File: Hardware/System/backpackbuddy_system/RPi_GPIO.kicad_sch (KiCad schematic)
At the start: 1 part, among them J6 RPi_GPIO

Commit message: pin matched everything
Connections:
- net 3v3: now reaches J6.1 (Pin_1)
- net 3v3: now also J6.17 (Pin_17)
- net GPIO15_RXD: now reaches J6.10 (Pin_10)
- net GPIO17: now reaches J6.11 (Pin_11)
- net GPIO18_PCM_CLK: now reaches J6.12 (Pin_12)
- net GPIO27: now reaches J6.13 (Pin_13)
- net GND: now reaches J6.14 (Pin_14)
- net GND: now also J6.20 (Pin_20), J6.25 (Pin_25), J6.30 (Pin_30), J6.34 (Pin_34), J6.39 (Pin_39), J6.6 (Pin_6), J6.9 (Pin_9)
- net GPIO22: now reaches J6.15 (Pin_15)
- net GPIO23: now reaches J6.16 (Pin_16)
- net GPIO24: now reaches J6.18 (Pin_18)
- net GPIO10_MOSI: now reaches J6.19 (Pin_19)
- net 5v: now reaches J6.2 (Pin_2)
- net 5v: now also J6.4 (Pin_4)
- net GPIO10_MISO: now reaches J6.21 (Pin_21)
- net GPIO25: now reaches J6.22 (Pin_22)
- net GPIO11_SCLK: now reaches J6.23 (Pin_23)
- net GPIO8_CE0: now reaches J6.24 (Pin_24)
- net GPIO7_CE1: now reaches J6.26 (Pin_26)
- net GPIO0_ID_SD: now reaches J6.27 (Pin_27)
- net GPIO1_ID_SE: now reaches J6.28 (Pin_28)
- net GPIO5: now reaches J6.29 (Pin_29)
- net GPIO6: now reaches J6.31 (Pin_31)
- net GPIO12_PWM0: now reaches J6.32 (Pin_32)
- net GPIO13_PWM1: now reaches J6.33 (Pin_33)
- net GPIO19_PCM_FS: now reaches J6.35 (Pin_35)
- net GPIO16: now reaches J6.36 (Pin_36)
- net GPIO26: now reaches J6.37 (Pin_37)
- net GPIO20_PCM_DIN: now reaches J6.38 (Pin_38)
- net GPIO21_PCM_DOUT: now reaches J6.40 (Pin_40)
- net GPIO14_TXD: now reaches J6.8 (Pin_8)

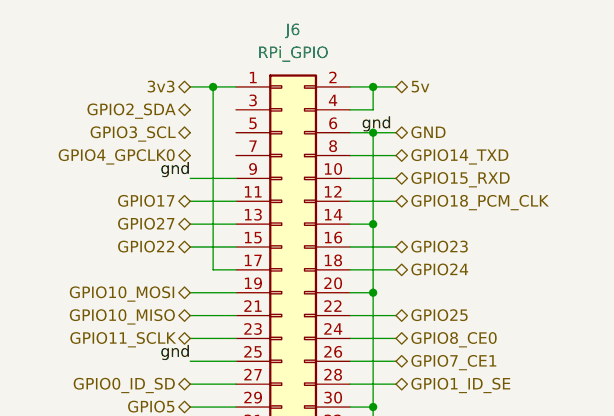
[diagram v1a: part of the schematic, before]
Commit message: pull down resistor to ESP reset
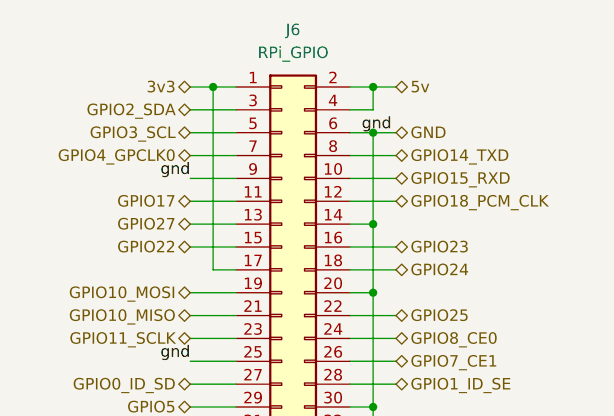
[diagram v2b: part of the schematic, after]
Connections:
- net GPIO2_SDA: now also J6.3 (Pin_3)
- net GPIO3_SCL: now also J6.5 (Pin_5)
- net GPIO4_GPCLK0: now also J6.7 (Pin_7)
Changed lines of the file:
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@@
+    (stroke (width 0) (type default) (color 0 0 0 0))
+  )
+  (wire (pts (xy 134.62 68.58) (xy 139.7 68.58))
     (stroke (width 0) (type default) (color 0 0 0 0))
   )
@@
     (stroke (width 0) (type default) (color 0 0 0 0))
   )
+  (wire (pts (xy 134.62 66.04) (xy 139.7 66.04))
+    (stroke (width 0) (type default) (color 0 0 0 0))
+  )
   (wire (pts (xy 152.4 63.5) (xy 154.94 63.5))
     (stroke (width 0) (type default) (color 0 0 0 0))
@@
     (stroke (width 0) (type default) (color 0 0 0 0))
   )
+  (wire (pts (xy 134.62 71.12) (xy 139.7 71.12))
+    (stroke (width 0) (type default) (color 0 0 0 0))
+  )

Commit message: decoupling caps
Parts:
- added C? (x4): 10uF, Capacitor_SMD:C_0805_2012Metric_Pad1.18x1.45mm_HandSolder, symbol Device:C
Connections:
- net GND: now also C?.2, C?.2, C?.2, C?.2
- new net +3V3: C?.1, C?.1
- new net +5V: C?.1, C?.1
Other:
- note added: "PI DECOUPLING CAPS"

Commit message: board outline redo
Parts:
- removed C?: 10uF, Capacitor_SMD:C_0805_2012Metric_Pad1.18x1.45mm_HandSolder, symbol Device:C
- gave numbers to parts that had none: 3
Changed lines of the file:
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@@
   (junction (at 154.94 86.36) (diameter 0) (color 0 0 0 0)
   )
-  (junction (at 187.96 40.64) (diameter 0) (color 0 0 0 0)
-  )
-  (junction (at 198.12 53.34) (diameter 0) (color 0 0 0 0)
-  )
   (wire (pts (xy 134.62 99.06) (xy 139.7 99.06))
     (stroke (width 0) (type default) (color 0 0 0 0))
@@
     (stroke (width 0) (type default) (color 0 0 0 0))
   )
-  (wire (pts (xy 198.12 50.8) (xy 198.12 53.34))
-    (stroke (width 0) (type default) (color 0 0 0 0))
-  )
-  (wire (pts (xy 187.96 39.37) (xy 187.96 40.64))
-    (stroke (width 0) (type default) (color 0 0 0 0))
-  )
   (wire (pts (xy 152.4 104.14) (xy 154.94 104.14))
     (stroke (width 0) (type default) (color 0 0 0 0))
@@
     (stroke (width 0) (type default) (color 0 0 0 0))
   )
-  (wire (pts (xy 187.96 40.64) (xy 187.96 43.18))
+  (wire (pts (xy 187.96 39.37) (xy 187.96 43.18))
     (stroke (width 0) (type default) (color 0 0 0 0))
   )
@@
     (stroke (width 0) (type default) (color 0 0 0 0))
   )
-  (wire (pts (xy 187.96 53.34) (xy 198.12 53.34))
-    (stroke (width 0) (type default) (color 0 0 0 0))
-  )
   (wire (pts (xy 152.4 91.44) (xy 157.48 91.44))
     (stroke (width 0) (type default) (color 0 0 0 0))
@@
     (stroke (width 0) (type default) (color 0 0 0 0))
   )
-  (wire (pts (xy 198.12 53.34) (xy 203.2 53.34))
+  (wire (pts (xy 187.96 53.34) (xy 203.2 53.34))
     (stroke (width 0) (type default) (color 0 0 0 0))
   )
@@
     (stroke (width 0) (type default) (color 0 0 0 0))
   )
-  (wire (pts (xy 198.12 40.64) (xy 187.96 40.64))
-    (stroke (width 0) (type default) (color 0 0 0 0))
-  )
   (wire (pts (xy 152.4 66.04) (xy 154.94 66.04))
     (stroke (width 0) (type default) (color 0 0 0 0))
@@
   )
   (wire (pts (xy 152.4 63.5) (xy 154.94 63.5))
-    (stroke (width 0) (type default) (color 0 0 0 0))
-  )
-  (wire (pts (xy 198.12 40.64) (xy 198.12 43.18))
     (stroke (width 0) (type default) (color 0 0 0 0))
   )
@@
   (symbol (lib_id "Device:C") (at 187.96 46.99 0) (unit 1)
     (in_bom yes) (on_board yes)
-    (property "Reference" "C?" (id 0) (at 181.61 46.99 0)
+    (property "Reference" "C23" (id 0) (at 181.61 46.99 0)
       (effects (font (size 1.27 1.27)) (justify left))
     )
@@
   (symbol (lib_id "power:GND") (at 203.2 54.61 0) (unit 1)
     (in_bom yes) (on_board yes) (fields_autoplaced)
-    (property "Reference" "#PWR?" (id 0) (at 203.2 60.96 0)
+    (property "Reference" "#PWR044" (id 0) (at 203.2 60.96 0)
       (effects (font (size 1.27 1.27)) hide)
     )
@@
   (symbol (lib_id "Device:C") (at 208.28 46.99 0) (unit 1)
     (in_bom yes) (on_board yes)
-    (property "Reference" "C?" (id 0) (at 201.93 46.99 0)
+    (property "Reference" "C24" (id 0) (at 201.93 46.99 0)
       (effects (font (size 1.27 1.27)) (justify left))
     )
@@
     (pin "9")
   )
-  (symbol (lib_id "Device:C") (at 198.12 46.99 0) (unit 1)
-    (in_bom yes) (on_board yes)
-    (property "Reference" "C?" (id 0) (at 191.77 46.99 0)
-      (effects (font (size 1.27 1.27)) (justify left))
-    )
-    (property "Value" "10uF" (id 1) (at 191.77 49.53 0)
-      (effects (font (size 1.27 1.27)) (justify left))
-    )
-    (property "Footprint" "Capacitor_SMD:C_0805_2012Metric_Pad1.18x1.45mm_HandSolder" (id 2) (at 199.0852 50.8 0)
-      (effects (font (size 1.27 1.27)) hide)
-    )
-    (property "Datasheet" "~" (id 3) (at 198.12 46.99 0)
-      (effects (font (size 1.27 1.27)) hide)
-    )
-    (property "MPN" "CAP CER 10UF 25V X5R 0805" (id 4) (at 198.12 46.99 0)
-      (effects (font (size 1.27 1.27)) hide)
-    )
-    (property "Stock" "https://www.digikey.com/en/products/detail/kyocera-avx/08053D106KAT4A/12153448?utm_adgroup=Capacitors&utm_source=google&utm_medium=cpc&utm_campaign=Shopping_Supplier_AVX%20Corporation&utm_term=&utm_content=Capacitors" (id 5) (at 198.12 46.99 0)
-      (effects (font (size 1.27 1.27)) hide)
-    )
-    (pin "1")
-    (pin "2")
-  )
   (symbol (lib_id "Device:C") (at 218.44 46.99 0) (unit 1)
     (in_bom yes) (on_board yes)
-    (property "Reference" "C?" (id 0) (at 212.09 46.99 0)
+    (property "Reference" "C25" (id 0) (at 212.09 46.99 0)
       (effects (font (size 1.27 1.27)) (justify left))
     )
@@
   (symbol (lib_id "power:+3V3") (at 218.44 39.37 0) (unit 1)
     (in_bom yes) (on_board yes) (fields_autoplaced)
-    (property "Reference" "#PWR?" (id 0) (at 218.44 43.18 0)
+    (property "Reference" "#PWR045" (id 0) (at 218.44 43.18 0)
       (effects (font (size 1.27 1.27)) hide)
     )
@@
   (symbol (lib_id "power:+5V") (at 187.96 39.37 0) (unit 1)
     (in_bom yes) (on_board yes) (fields_autoplaced)
-    (property "Reference" "#PWR?" (id 0) (at 187.96 43.18 0)
-      (effects (font (size 1.27 1.27)) hide)
-    )
+    (property "Reference" "#PWR043" (id 0) (at 187.96 43.18 0)
+      (effects (font (size 1.27 1.27)) hide)
+    )

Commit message: almost done
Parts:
- removed C25: 10uF, Capacitor_SMD:C_0805_2012Metric_Pad1.18x1.45mm_HandSolder, symbol Device:C
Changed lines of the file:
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@@
   (junction (at 137.16 63.5) (diameter 0) (color 0 0 0 0)
   )
-  (junction (at 208.28 53.34) (diameter 0) (color 0 0 0 0)
-  )
   (junction (at 154.94 63.5) (diameter 0) (color 0 0 0 0)
   )
   (junction (at 154.94 78.74) (diameter 0) (color 0 0 0 0)
   )
-  (junction (at 218.44 40.64) (diameter 0) (color 0 0 0 0)
-  )
   (junction (at 154.94 68.58) (diameter 0) (color 0 0 0 0)
   )
@@
     (stroke (width 0) (type default) (color 0 0 0 0))
   )
-  (wire (pts (xy 218.44 53.34) (xy 218.44 50.8))
-    (stroke (width 0) (type default) (color 0 0 0 0))
-  )
   (wire (pts (xy 134.62 86.36) (xy 139.7 86.36))
     (stroke (width 0) (type default) (color 0 0 0 0))
@@
     (stroke (width 0) (type default) (color 0 0 0 0))
   )
-  (wire (pts (xy 208.28 53.34) (xy 218.44 53.34))
-    (stroke (width 0) (type default) (color 0 0 0 0))
-  )
   (wire (pts (xy 134.62 96.52) (xy 139.7 96.52))
     (stroke (width 0) (type default) (color 0 0 0 0))
   )
   (wire (pts (xy 187.96 50.8) (xy 187.96 53.34))
-    (stroke (width 0) (type default) (color 0 0 0 0))
-  )
-  (wire (pts (xy 218.44 40.64) (xy 218.44 43.18))
     (stroke (width 0) (type default) (color 0 0 0 0))
   )
@@
     (pin "9")
   )
-  (symbol (lib_id "Device:C") (at 218.44 46.99 0) (unit 1)
-    (in_bom yes) (on_board yes)
-    (property "Reference" "C25" (id 0) (at 212.09 46.99 0)
-      (effects (font (size 1.27 1.27)) (justify left))
-    )
-    (property "Value" "10uF" (id 1) (at 212.09 49.53 0)
-      (effects (font (size 1.27 1.27)) (justify left))
-    )
-    (property "Footprint" "Capacitor_SMD:C_0805_2012Metric_Pad1.18x1.45mm_HandSolder" (id 2) (at 219.4052 50.8 0)
-      (effects (font (size 1.27 1.27)) hide)
-    )
-    (property "Datasheet" "~" (id 3) (at 218.44 46.99 0)
-      (effects (font (size 1.27 1.27)) hide)
-    )
-    (property "MPN" "CAP CER 10UF 25V X5R 0805" (id 4) (at 218.44 46.99 0)
-      (effects (font (size 1.27 1.27)) hide)
-    )
-    (property "Stock" "https://www.digikey.com/en/products/detail/kyocera-avx/08053D106KAT4A/12153448?utm_adgroup=Capacitors&utm_source=google&utm_medium=cpc&utm_campaign=Shopping_Supplier_AVX%20Corporation&utm_term=&utm_content=Capacitors" (id 5) (at 218.44 46.99 0)
-      (effects (font (size 1.27 1.27)) hide)
-    )
-    (pin "1")
-    (pin "2")
-  )
   (symbol (lib_id "power:+3V3") (at 218.44 39.37 0) (unit 1)
